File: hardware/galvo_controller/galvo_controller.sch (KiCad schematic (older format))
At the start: 117 parts, among them J1 USB_OTG, J2 Conn_01x03, J3 Conn_01x03, J4 Micro_SD_Card_Det, J5 Red, J6 White, J7 Conn_01x03, J8 Conn_01x03, Q1 MMBT2222, Q2 MMBT2222, U1 SN74LV1T34, U2 ESP-WROOM-32D, U3 CP2104, U4 TPS54295PWP, U5 PCM3060, U6 NCP1117LP, U7 OPA2134, U8 LME49724, U9 LME49724

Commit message: Added oled display
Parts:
- added C51, C52, C54, C55: 1u, Capacitors_SMD:C_0805, symbol C
- added C53, C56: 10u, Capacitors_SMD:C_0805, symbol C
- added R40: 390k, Resistors_SMD:R_0603, symbol R
- added U10: UG-2832HSWEG02, footprint:UG-2832HSWEG02, symbol UG-2832HSWEG02
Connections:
- net labels added: OLED_RST
- wire segments 404 -> 437
- no-connect marks 5 -> 6
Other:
- moved on the sheet: C1, C10, C11, C12, C13, C14, C15, C16, C17, C18, C19, C2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

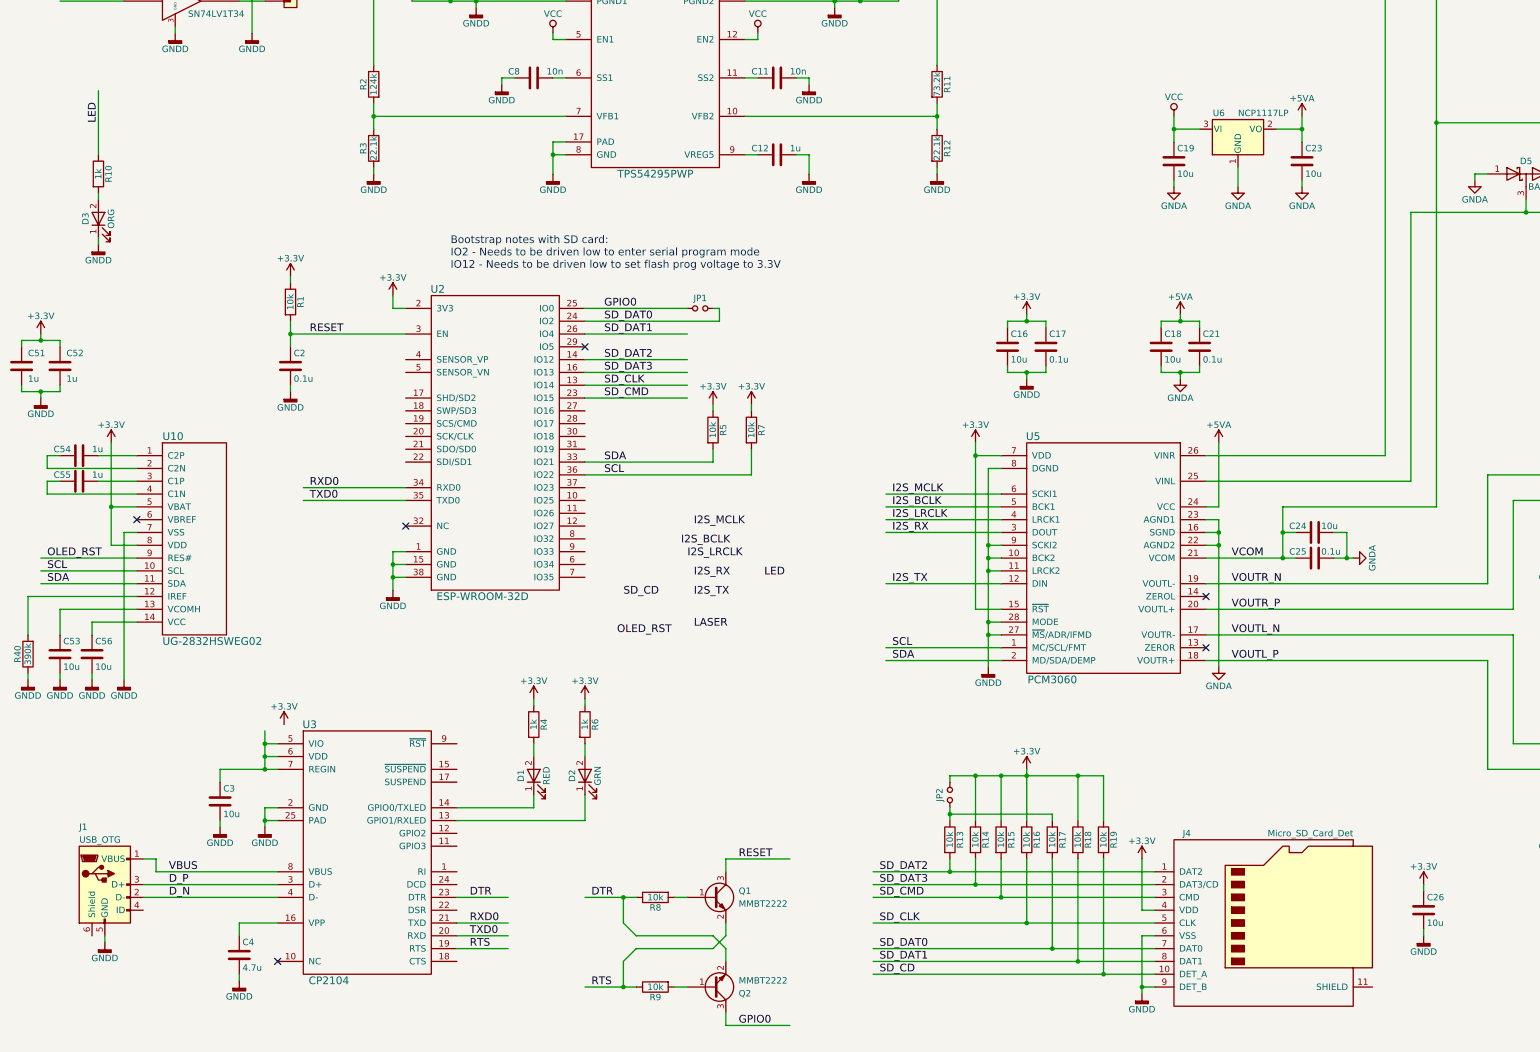
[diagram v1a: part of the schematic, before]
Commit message: Adding directional switch
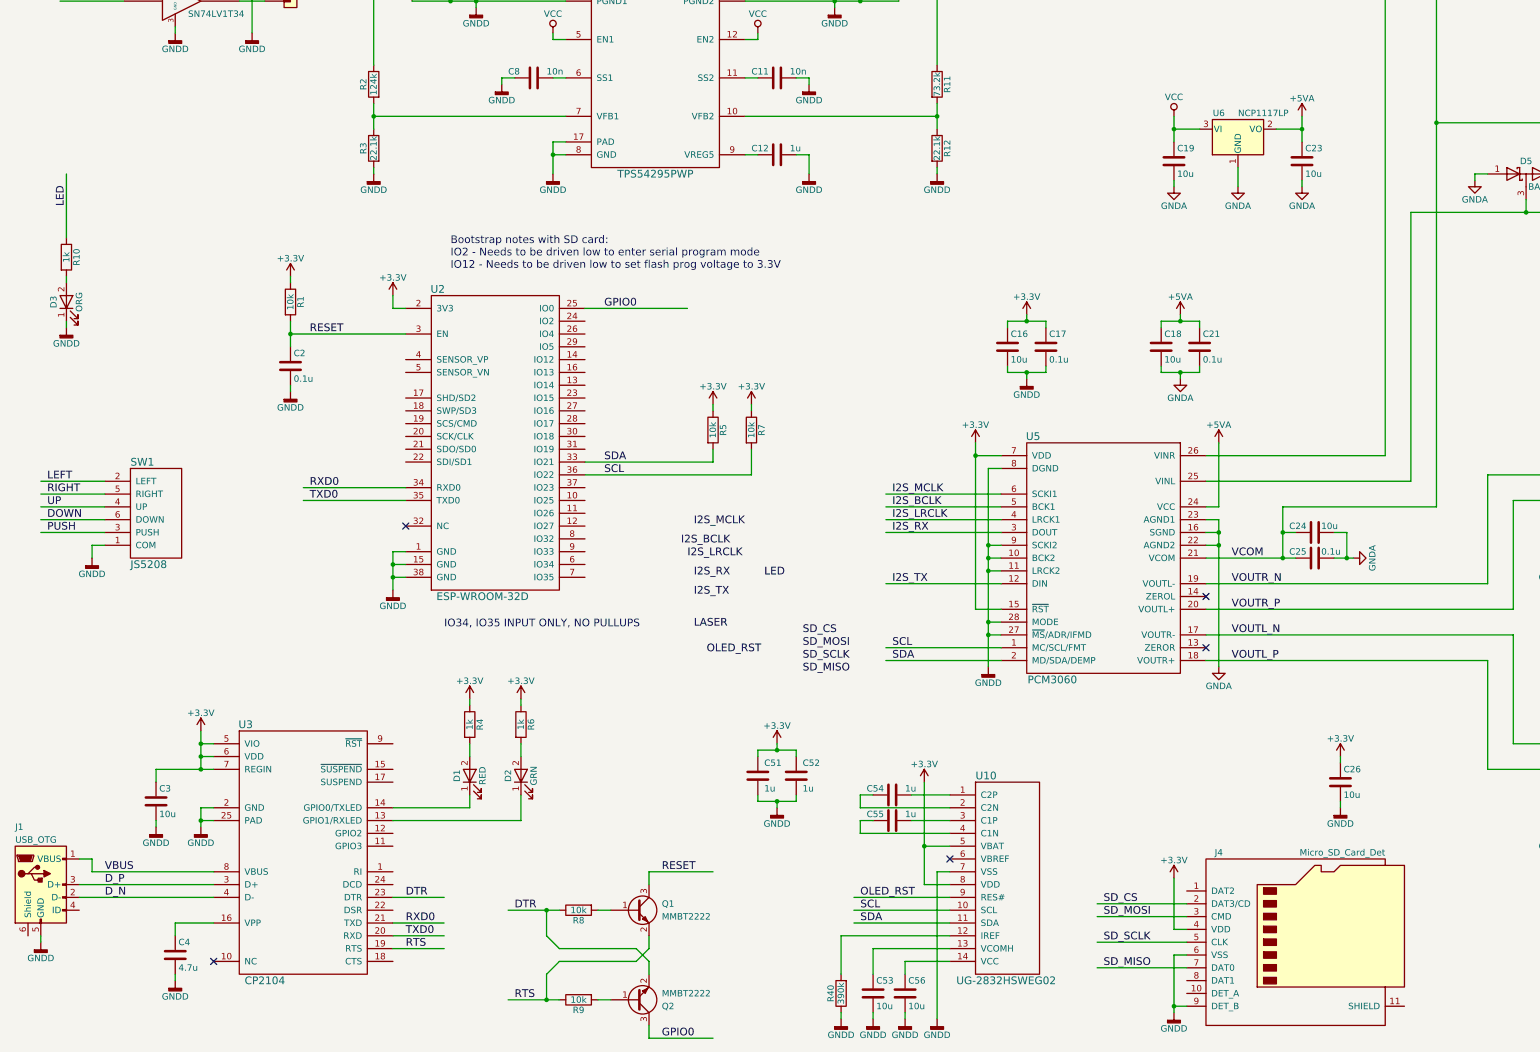
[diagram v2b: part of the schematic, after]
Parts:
- removed JP1, JP2: Jumper_NO_Small, Pin_Headers:Pin_Header_Straight_1x02_Pitch2.54mm, symbol Jumper_NO_Small
- removed R13, R14, R15, R16, R17, R18, R19: 10k, Resistors_SMD:R_0603, symbol R
- added SW1: JS5208, footprint:JS5208, symbol JS5208
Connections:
- net labels added: DOWN, LEFT, PUSH, RIGHT, SD_CS, SD_MISO, SD_MOSI, SD_SCLK, UP
- net labels removed: SD_CD, SD_CLK, SD_CMD, SD_DAT0, SD_DAT1, SD_DAT2, SD_DAT3
- wire segments 437 -> 416
- no-connect marks 6 -> 5
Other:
- note added: "IO34, IO35 INPUT ONLY, NO PULLUPS"
- moved on the sheet: C26, C3, C4, C51, C52, C53, C54, C55, C56, D1, D2, D3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

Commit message: Added oled display (reverted from commit 7e9d64baadf71845b197ee83ec8b18551d687449)
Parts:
- removed C51, C52, C54, C55: 1u, Capacitors_SMD:C_0805, symbol C
- removed C53, C56: 10u, Capacitors_SMD:C_0805, symbol C
- removed R40: 390k, Resistors_SMD:R_0603, symbol R
- removed SW1: JS5208, footprint:JS5208, symbol JS5208
- removed U10: UG-2832HSWEG02, footprint:UG-2832HSWEG02, symbol UG-2832HSWEG02
- added JP1, JP2: Jumper_NO_Small, Pin_Headers:Pin_Header_Straight_1x02_Pitch2.54mm, symbol Jumper_NO_Small
- added R13, R14, R15, R16, R17, R18, R19: 10k, Resistors_SMD:R_0603, symbol R
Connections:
- net labels added: SD_CD, SD_CLK, SD_CMD, SD_DAT0, SD_DAT1, SD_DAT2, SD_DAT3
- net labels removed: DOWN, LEFT, OLED_RST, PUSH, RIGHT, SD_CS, SD_MISO, SD_MOSI, SD_SCLK, UP
- wire segments 416 -> 404
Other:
- note removed: "IO34, IO35 INPUT ONLY, NO PULLUPS"
- moved on the sheet: C1, C10, C11, C12, C13, C14, C15, C16, C17, C18, C19, C2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

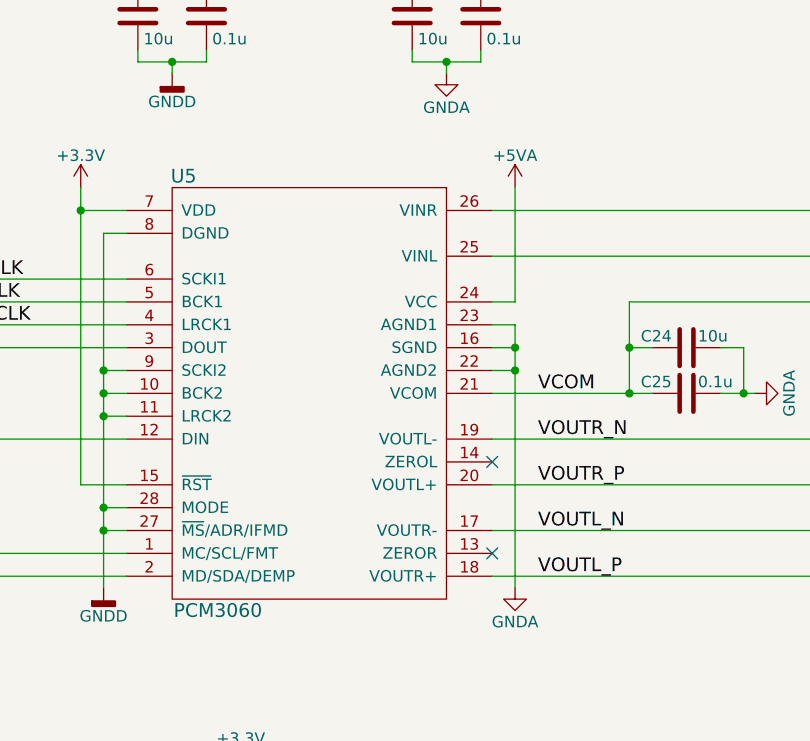
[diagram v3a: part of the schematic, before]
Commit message: Swapped input L/R channels
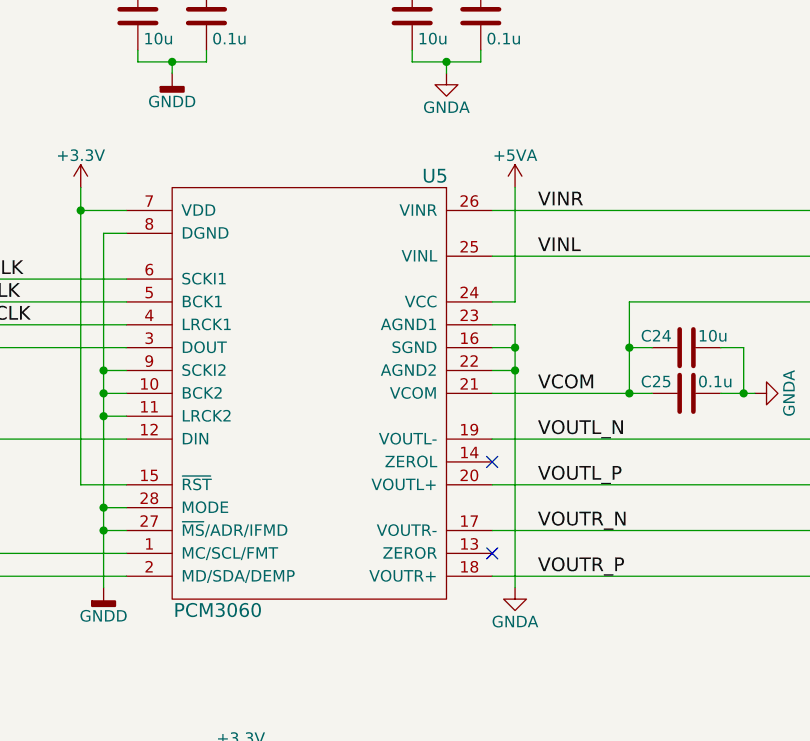
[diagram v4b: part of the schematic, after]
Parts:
- U5: footprint Housings_SSOP:TSSOP-28_4.4x9.7mm_Pitch0.65mm -> (none); Part 296-38201-1-ND -> (none); Source DigiKey -> (none)
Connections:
- net labels added: VINL, VINR
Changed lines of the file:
@@
 $EndComp
 $Comp
-L PCM3060 U5
-U 1 1 5A9F9297
-P 9100 6350
-F 0 "U5" H 9650 7300 60  0000 C CNN
-F 1 "PCM3060" H 9500 5400 60  0000 C CNN
-F 2 "Housings_SSOP:TSSOP-28_4.4x9.7mm_Pitch0.65mm" H 9100 6350 60  0001 C CNN
-F 3 "" H 9100 6350 60  0001 C CNN
-F 4 "DigiKey" H 9100 6350 60  0001 C CNN "Source"
-F 5 "296-38201-1-ND" H 9100 6350 60  0001 C CNN "Part"
-	1    9100 6350
-	-1   0    0    -1
-$EndComp
-$Comp
 L VEE #PWR70
 U 1 1 5A9F997F
@@
 	1    0    0    -1
 $EndComp
-Text Label 10100 6550 0    60   ~ 0
+Text Label 10100 6950 0    60   ~ 0
 VOUTR_N
-Text Label 10100 6750 0    60   ~ 0
+Text Label 10100 7150 0    60   ~ 0
 VOUTR_P
-Text Label 10100 6950 0    60   ~ 0
+Text Label 10100 6550 0    60   ~ 0
 VOUTL_N
-Text Label 10100 7150 0    60   ~ 0
+Text Label 10100 6750 0    60   ~ 0
 VOUTL_P
 Text Label 14600 5750 0    60   ~ 0
@@
 	8400 8400 8400 8050
 Connection ~ 8400 8050
+$Comp
+L PCM3060 U5
+U 1 1 5AA91202
+P 9100 6350
+F 0 "U5" H 8550 7300 60  0000 C CNN
+F 1 "PCM3060" H 9500 5400 60  0000 C CNN
+F 2 "" H 9100 6350 60  0001 C CNN
+F 3 "" H 9100 6350 60  0001 C CNN
+	1    9100 6350
+	-1   0    0    -1
+$EndComp
+Text Label 10100 5550 0    60   ~ 0
+VINR
+Text Label 10100 5750 0    60   ~ 0
+VINL
 $EndSCHEMATC

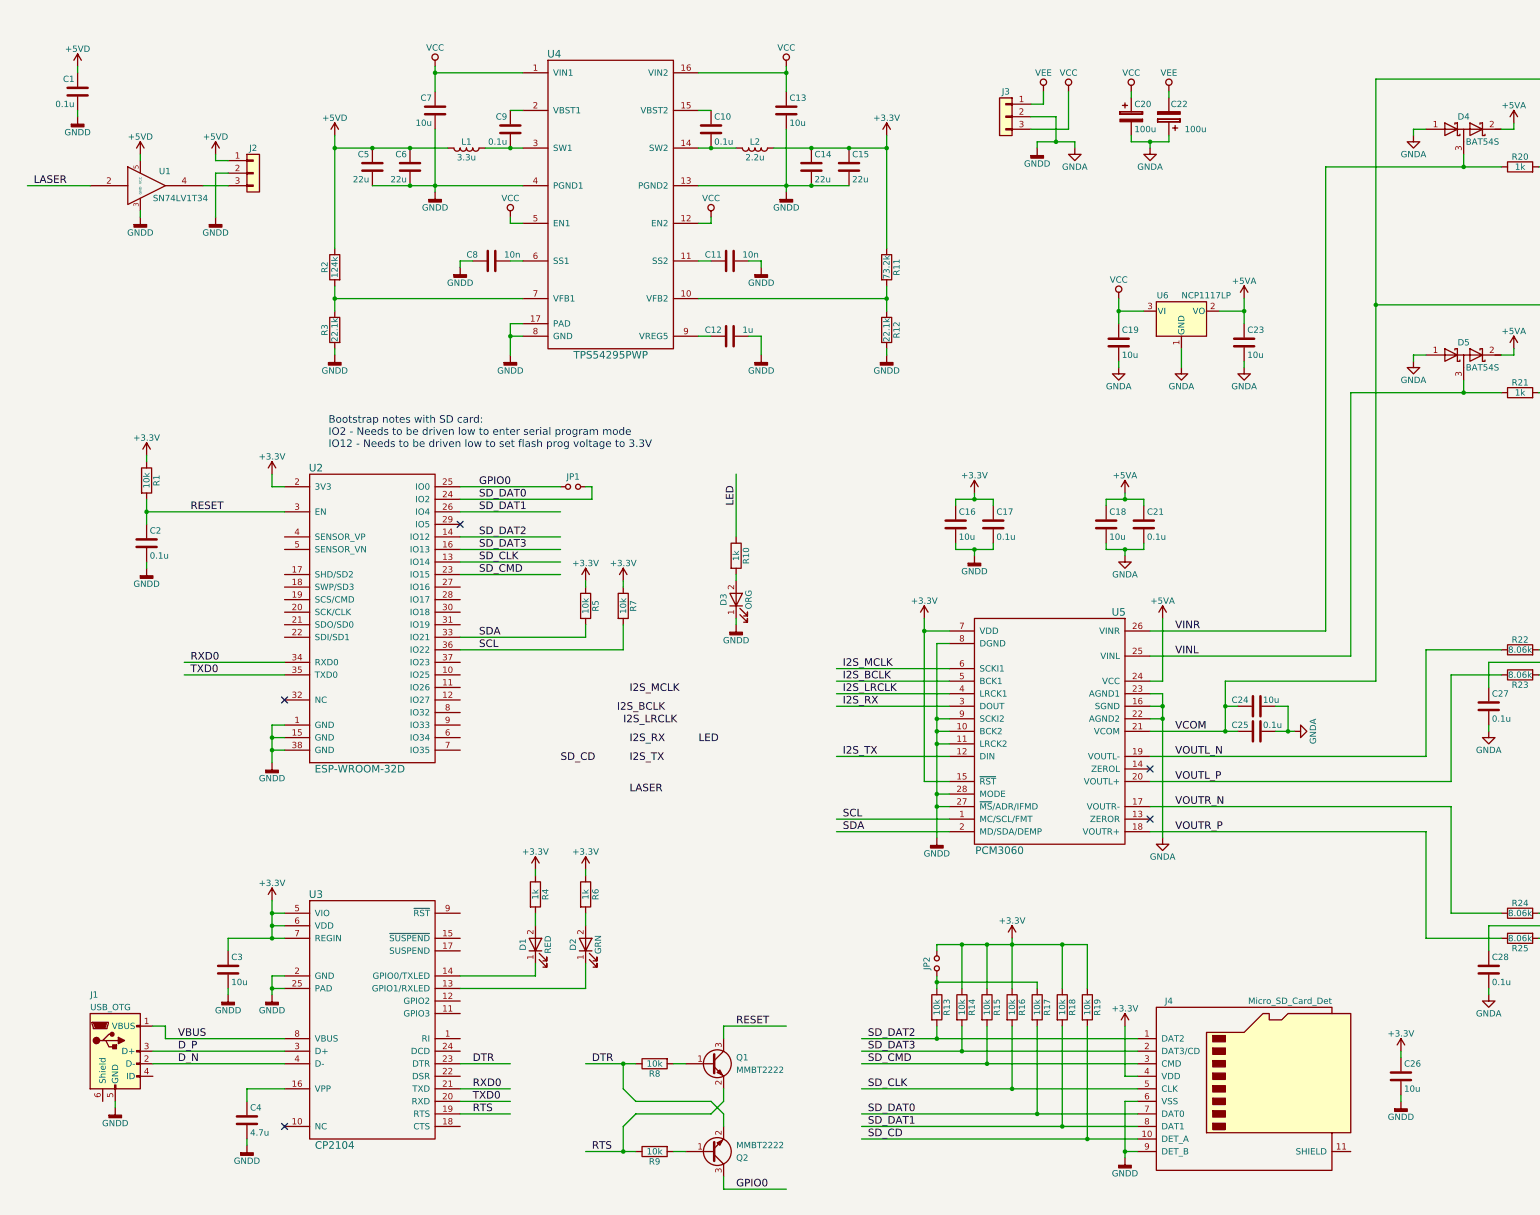
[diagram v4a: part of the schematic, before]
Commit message: Added OLED and nav switch
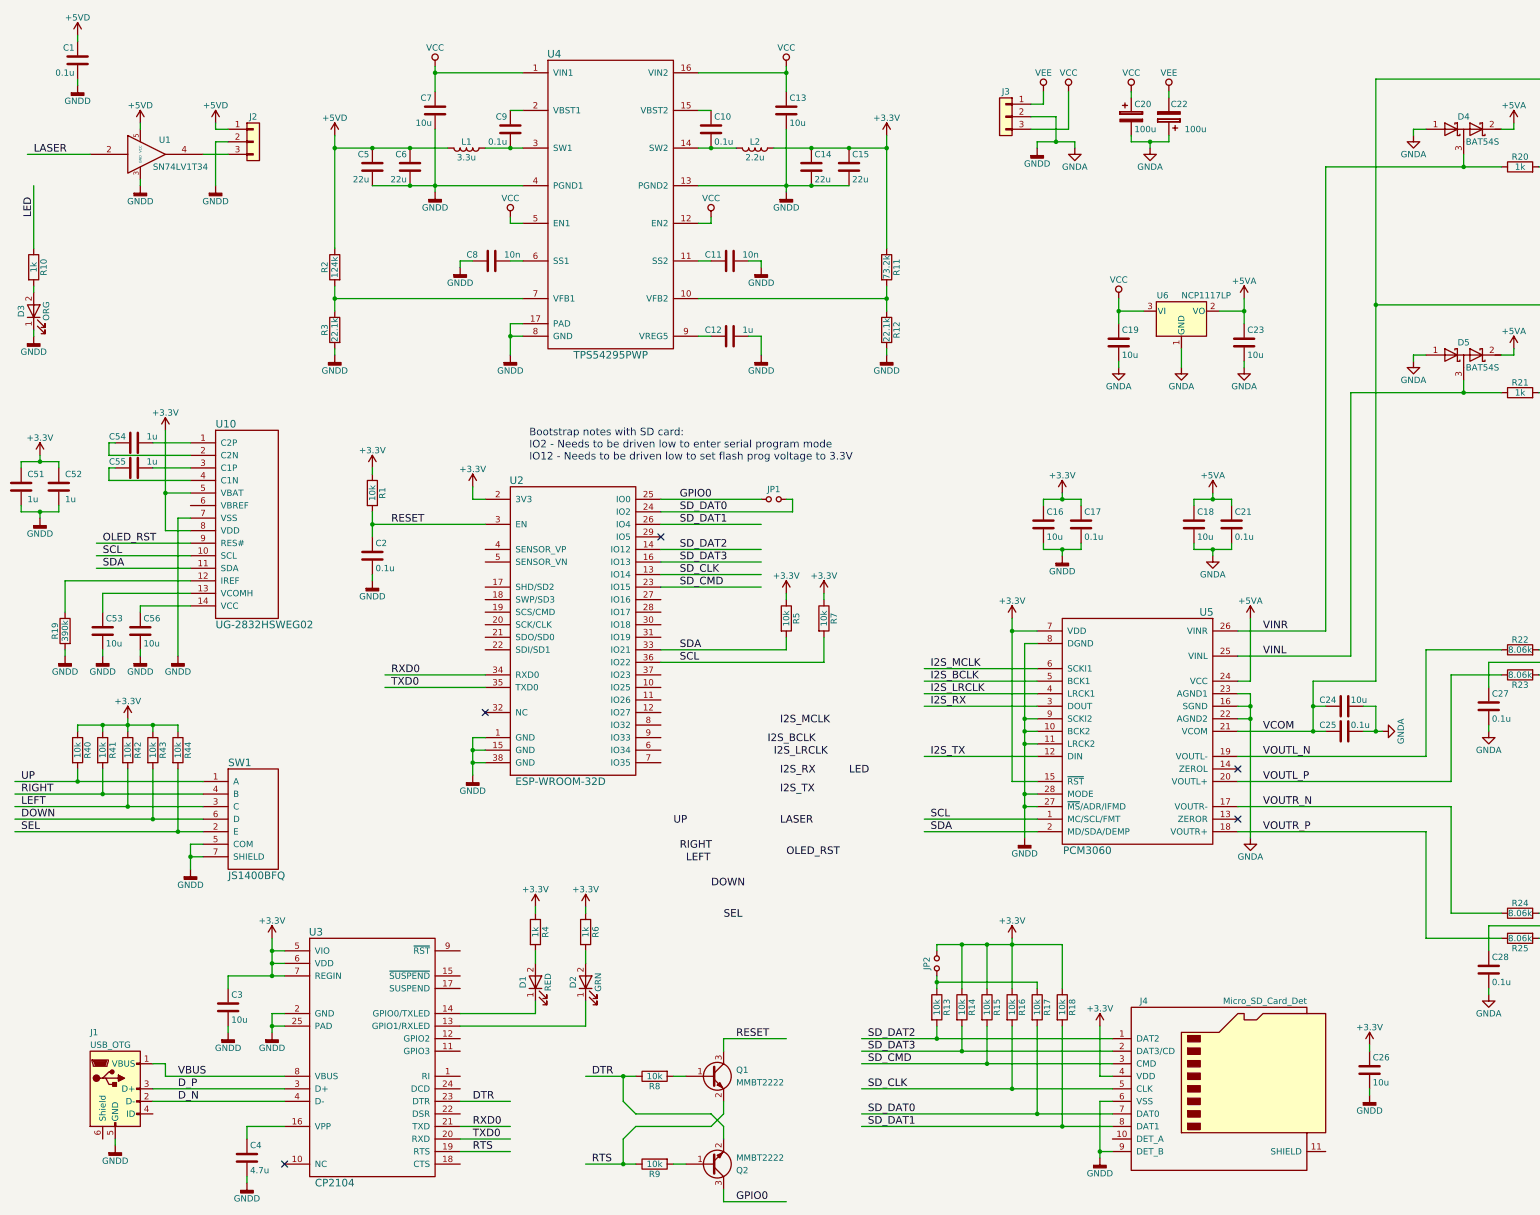
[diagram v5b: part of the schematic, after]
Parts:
- added C51, C52, C54, C55: 1u, Capacitors_SMD:C_0805, symbol C
- added C53, C56: 10u, Capacitors_SMD:C_0805, symbol C
- added R40, R41, R42, R43, R44: 10k, Resistors_SMD:R_0603, symbol R
- added SW1: JS1400BFQ, footprint:JS1400BFQ, symbol JS1400BFQ
- added U10: UG-2832HSWEG02, footprint:UG-2832HSWEG02, symbol UG-2832HSWEG02
- R19: value 10k -> 390k; Part 311-10.0KHRCT-ND -> 311-390KHRCT-ND
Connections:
- net labels added: DOWN, LEFT, OLED_RST, RIGHT, SEL, UP
- net labels removed: SD_CD
- wire segments 404 -> 453
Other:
- moved on the sheet: C1, C16, C17, C18, C2, C21, C24, C25, C26, C3, C4, D1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

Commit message: Re-annotated schematic
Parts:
- renumbered C51 to C1, C5 to C10, C2 to C11, C6 to C12, C7 to C13, C8 to C14, C9 to C15, C10 to C16, C11 to C17, C12 to C18, C13 to C19, C52 to C2, C14 to C20, C15 to C21, C16 to C22, C17 to C23, C19 to C24, C20 to C25, C22 to C26, C18 to C27, C21 to C28, C23 to C29, C1 to C3, C24 to C30, C25 to C31, C26 to C32, C27 to C33, C28 to C34, C29 to C35, C30 to C36, C31 to C37, C32 to C38, C33 to C39, C53 to C4, C34 to C40, C35 to C41, C36 to C42, C37 to C43, C38 to C44, C39 to C45, C40 to C46, C41 to C47, C42 to C48, C43 to C49, C54 to C5, C44 to C50, C45 to C51, C46 to C52, C47 to C53, C48 to C54, C49 to C55, C50 to C56, C55 to C6, C56 to C7, C3 to C8, C4 to C9, D3 to D1, D1 to D2, D2 to D3, R10 to R1, R1 to R10, R4 to R11, R6 to R12, R8 to R13, R9 to R14, R5 to R15, R7 to R16, R11 to R17, R12 to R18, R13 to R19, R19 to R2, R14 to R20, R15 to R21, R16 to R22, R17 to R23, R18 to R24, R20 to R25, R21 to R26, R22 to R27, R23 to R28, R24 to R29, R40 to R3, R25 to R30, R26 to R31, R27 to R32, R28 to R33, R29 to R34, R30 to R35, R31 to R36, R32 to R37, R33 to R38, R34 to R39, R41 to R4, R35 to R40, R36 to R41, R37 to R42, R38 to R43, R39 to R44, R42 to R5, R43 to R6, R44 to R7, R2 to R8, R3 to R9, U9 to U10, U10 to U2, U2 to U4, U4 to U5, U5 to U6, U6 to U7, U7 to U8, U8 to U9

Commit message: Working on layout
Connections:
- wire segments 453 -> 455
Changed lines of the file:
@@
 Text Label 7000 7350 0    60   ~ 0
 OLED_RST
+$Comp
+L GNDD #PWR?
+U 1 1 5AA9C995
+P 11400 9750
+F 0 "#PWR?" H 11400 9500 50  0001 C CNN
+F 1 "GNDD" H 11400 9625 50  0000 C CNN
+F 2 "" H 11400 9750 50  0001 C CNN
+F 3 "" H 11400 9750 50  0001 C CNN
+	1    11400 9750
+	1    0    0    -1
+$EndComp
+Wire Wire Line
+	11300 9700 11400 9700
+Wire Wire Line
+	11400 9700 11400 9750
 $EndSCHEMATC
